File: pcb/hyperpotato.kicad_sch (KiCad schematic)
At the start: 38 parts, among them J1 Conn_01x02_Socket, J2 Conn_01x03_Pin, Q1 AO3401A, SW1 SW_Push_45deg, SW10 SW_Push_45deg, SW11 SW_Push_45deg, SW12 SW_Push_45deg, SW13 SW_Push_45deg, SW14 SW_SPDT, SW15 SW_Push, SW2 SW_Push_45deg, SW3 SW_Push_45deg, SW4 SW_Push_45deg, SW5 SW_Push_45deg, SW6 SW_Push_45deg, SW7 SW_Push_45deg, SW8 SW_Push_45deg, SW9 SW_Push_45deg, U1 Seeeduino Xiao nRF52840, U2 SK8707-01-SENSOR, U3 SK8707-01, U4 DRV2605LDGS

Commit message: Start back with e73 module
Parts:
- removed D1, D10, D11, D12, D13, D2, D3, D4, D5, D6, D7, D8, D9: D_Small, ssbb_parts:D_1206_HandSolder_reversible, symbol Device:D_Small
- removed J1: Conn_01x02_Socket, ssbb_parts:JST_PH_S2B-PH-K_Horizontal_reversible, symbol Connector:Conn_01x02_Socket
- removed SW10, SW12: SW_Push_45deg, ssbb_parts:SW_choc_v1_reversible_1u, symbol Switch:SW_Push_45deg
- removed SW13: SW_Push_45deg, ssbb_parts:SW_choc_v1_reversible_1.5u, symbol Switch:SW_Push_45deg
- removed SW14: SW_SPDT, ssbb_parts:SW_SPDT_PCM12_reversible, symbol Switch:SW_SPDT
- removed SW15: SW_Push, ssbb_parts:Panasonic_EVQPUL_EVQPUC_reversible, symbol Switch:SW_Push
- removed U1: Seeeduino Xiao nRF52840, ssbb_parts:Xiao_nRF52840_AC_Reflow_reversible, symbol PCM_marbastlib-promicroish:Seeeduino_Xiao_nRF52840
- removed U2: SK8707-01-SENSOR, ssbb_parts:Sprintek_SK8707-01_Sensor, symbol ssbb_parts:Sprintek_SK8707-01_Sensor
- removed U3: SK8707-01, symbol ssbb_parts:Sprintek_SK8707–01
- added C1, C12: 100n, Capacitor_SMD:C_0402_1005Metric, symbol Device:C_Small
- added C10, C11, C7, C8, C9: 4u7, Capacitor_SMD:C_0402_1005Metric, symbol Device:C_Small
- added C4, C5: 12p, Capacitor_SMD:C_0402_1005Metric, symbol Device:C_Small
- added C6: 1u, Capacitor_SMD:C_0402_1005Metric, symbol Device:C_Small
- added D1: BSD3C051V, Diode_SMD:D_SOD-323, symbol Device:D_TVS
- added D2: LED_ARGB, symbol Device:LED_ARGB
- added F1: 750 mA, Fuse:Fuse_0603_1608Metric, symbol Device:Fuse_Small
- added J1: HRO_TYPE-C-31-M-14, Connector_USB:USB_C_Receptacle_HRO_TYPE-C-31-M-12, symbol Connector:USB_C_Receptacle_USB2.0
- added J3: Conn_01x04_Socket, symbol Connector:Conn_01x04_Socket
- added J4: Battery, PCM_marbastlib-various:Molex_Pico-EZmate_78171-0002_1x02-1MP_P1.20mm_Vertical, symbol Connector_Generic_MountingPin:Conn_01x02_MountingPin
- added L1, L2: BLM15PX121SN1D, Inductor_SMD:L_0402_1005Metric, symbol Device:L_Small
- added L3: 10 uH, Inductor_SMD:L_0603_1608Metric, symbol Device:L_Small
- added LED1: orange, LED_SMD:LED_0402_1005Metric, symbol Device:LED_Small
- added Q2: 2N7002, Package_TO_SOT_SMD:SOT-23, symbol Transistor_FET:2N7002
- added Q3: AO3401A, Package_TO_SOT_SMD:SOT-23, symbol Transistor_FET:AO3401A
- added R1, R2: 5k1, Resistor_SMD:R_0402_1005Metric, symbol Device:R_Small
- added R10, R7: 1k5, Resistor_SMD:R_0402_1005Metric, symbol Device:R_Small
- added R11: 100R, Resistor_SMD:R_0402_1005Metric, symbol Device:R_Small
- added R12, R9: 10k, Resistor_SMD:R_0402_1005Metric, symbol Device:R_Small
- added R13, R14: 4.7k, symbol Device:R_Small
- added R15: 100k, Resistor_SMD:R_0402_1005Metric, symbol Device:R_Small
- added R16: 2M, Resistor_SMD:R_0805_2012Metric, symbol Device:R_Small
- added R17, R18, R19: 1k5, symbol Device:R_Small
- added R3, R4: 5.1k, symbol Device:R_Small
- added R6: 47k, Resistor_SMD:R_0402_1005Metric, symbol Device:R_Small
- added R8: 3k9, Resistor_SMD:R_0402_1005Metric, symbol Device:R_Small
- added SW1: RST, PCM_marbastlib-various:SW_SPST_SKQG_WithStem, symbol Switch:SW_Push_45deg
- added SW14, SW2, SW8: SW_Push_45deg, symbol Switch:SW_Push_45deg
- added SW15: PWR, PCM_marbastlib-various:SW_MSK12C02-HB, symbol Switch:SW_Push_SPDT
- added U1: nRF52840_E73-2G4M08S1C, PCM_marbastlib-various:nRF52840_E73-2G4M08S1C, symbol PCM_marbastlib-various:nRF52840_E73-2G4M08S1C
- added U3: SRV05-4, Package_TO_SOT_SMD:SOT-23-6, symbol Power_Protection:SRV05-4
- added U4: BQ24075, Package_DFN_QFN:VQFN-16-1EP_3x3mm_P0.5mm_EP1.6x1.6mm, symbol Battery_Management:BQ24075RGT
- added U5: SK8707-01, symbol ssbb_parts:Sprintek_SK8707–01
- added U6: SK8707-01-SENSOR, ssbb_parts:Sprintek_SK8707-01_Sensor, symbol ssbb_parts:Sprintek_SK8707-01_Sensor
- added U7: MAX17048, Package_DFN_QFN:DFN-8-1EP_2x2mm_P0.5mm_EP0.7x1.3mm, symbol marbastlib-various:MAX17048
- added Y1: 32.768 KHz, Crystal:Crystal_SMD_2012-2Pin_2.0x1.2mm, symbol Device:Crystal_Small
- C2: renamed from C1; footprint ssbb_parts:C_1206_HandSolder_reversible -> (none)
- C3: renamed from C2; footprint ssbb_parts:C_1206_HandSolder_reversible -> (none)
- J2: value Conn_01x03_Pin -> ELV1411A
- SW10: renamed from SW8; footprint ssbb_parts:SW_choc_v1_reversible_1u -> (none)
- SW11, SW5, SW7: footprint ssbb_parts:SW_choc_v1_reversible_1u -> (none)
- SW12: renamed from SW4; footprint ssbb_parts:SW_choc_v1_reversible_1u -> (none)
- SW13: renamed from SW9; footprint ssbb_parts:SW_choc_v1_reversible_1u -> (none)
- SW3: renamed from SW1; footprint ssbb_parts:SW_choc_v1_reversible_1u -> (none)
- SW4: renamed from SW6; footprint ssbb_parts:SW_choc_v1_reversible_1u -> (none)
- SW6: renamed from SW2; footprint ssbb_parts:SW_choc_v1_reversible_1u -> (none)
- SW9: renamed from SW3; footprint ssbb_parts:SW_choc_v1_reversible_1u -> (none)
- renumbered R1 to R5, U4 to U2
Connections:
- net +3.3V: now also C6.1, D2.1 (A), J3.2 (Pin_2), L3.2, U1.19 (VDD)
- net +3V3: now also Q3.2 (S)
- net COL0: no longer SW5.1
- net COL1: no longer SW3.1, SW4.1
- net COL2: no longer SW11.1, SW6.1, SW7.1
- net COL3: no longer SW10.1, SW9.1
- net COL4: no longer SW12.1, SW13.1
- net GND: now also SW10.2, SW11.2, SW12.2, SW13.2, SW3.2, SW4.2, SW5.2, SW6.2, SW7.2, SW9.2, C1.2, C10.2, C11.2, C12.1, C4.2, C5.2, C6.2, C7.2, C8.2, C9.2, D1.1 (A1), J3.1 (Pin_1), J4.2 (Pin_2), J4.MP (MountPin), L1.2, Q2.2 (S), R1.1, R12.2, R16.1, R2.1, R6.2, R7.2, R8.2, R9.2, SW1.2, SW14.2, SW15.3 (C), SW2.2, SW8.2, U1.21 (GND), U1.24 (GND), U1.5 (GND), U3.2 (VN), U4.17 (VSS), U4.4 (~{CE}), U4.5 (EN2), U4.8 (VSS), U5.1 (GND), U7.1 (CTG), U7.4 (GND), U7.6 (QSTRT), U7.9 (GND); no longer U2.4 (IN/TRIG)
- net ROW1: no longer SW5.2
- net SCL: now also R4.2, U7.7 (SCL)
- net SDA: now also R3.2, U7.8 (SDA)
- net TP_CLK: now also R14.2, U5.3 (CLK)
- net TP_DATA: now also R13.2, U5.2 (DATA)
- net TP_S1: now also U5.9 (S1), U6.1 (S1)
- net TP_S2: now also U5.10 (S2), U6.2 (S2)
- net TP_S3: now also U5.11 (S3), U6.3 (S3)
- net TP_S4: now also U5.12 (S4), U6.4 (S4)
- net +3.3V_OPTIONAL renamed +3.3V_HAPTIC
- net +3.3V_HAPTIC: now also R3.1, R4.1
- net POWER_CUTOFF renamed HAPTIC_CUTOFF
- new net: J1.A5 (CC1), R2.2
- new net: C5.1, U1.13 (P0.01/XL2), Y1.1
- new net: C4.1, U1.11 (P0.00/XL1), Y1.2
- new net: F1.1, L2.2
- new net: J1.B5 (CC2), R1.2
- new net: Q2.1 (G), R11.2, R12.1
- new net: D2.2 (RK), R17.2
- new net: LED1.1 (K), R10.1
- new net: R10.2, U4.9 (~{CHG})
- new net: D2.3 (GK), R18.2
- new net: D2.4 (BK), R19.2
- new net: R15.2, SW15.1 (A)
- new net: R9.1, U4.1 (TS)
- new net: R8.1, U4.16 (ISET)
- new net +3.3V_TP: Q3.3 (D), R13.1, R14.1, U5.5 (VCC)
- new net +5V: C7.1, C8.1, F1.2, R11.1, U1.27 (VBUS), U3.5 (VP), U4.13 (IN)
- new net +BATT: C10.1, C12.2, J4.1 (Pin_1), R15.1, U4.2 (BAT), U4.3 (BAT), U7.2 (CELL), U7.3 (VDD)
- new net +VSW: C11.1, C9.1, LED1.2 (A), U1.23 (VDDH), U4.10 (OUT), U4.11 (OUT), U4.6 (EN1)
- new net ALERT: U7.5 (~{ALRT})
- new net DCCH: L3.1, U1.25 (DCCH)
- new net Earth: C1.1, D1.2 (A2), J1.A1 (GND), J1.A12 (GND), J1.B1 (GND), J1.B12 (GND), J1.S1 (SHIELD), L1.1
- new net HAPTIC_TRIGGER: U2.4 (IN/TRIG)
- new net ILIM: R7.1, U4.12 (ILIM)
- new net P.1.10: U1.2 (P1.10)
- new net P0.02: U1.7 (P0.02/AIN0)
- new net P0.03: U1.3 (P0.03/AIN1)
- new net P0.04: U1.18 (P0.04/AIN2)
- new net P0.05: U1.15 (P0.05/AIN3)
- new net P0.06: U1.14 (P0.06)
- new net P0.07: U1.22 (P0.07)
- new net P0.08: U1.16 (P0.08)
- new net P0.09: U1.41 (P0.09/NFC1)
- new net P0.10: U1.43 (P0.10/NFC2)
- new net P0.12: U1.20 (P0.12)
- new net P0.13: U1.33 (P0.13)
- new net P0.15: U1.28 (P0.15)
- new net P0.17: U1.30 (P0.17)
- new net P0.20: U1.32 (P0.20)
- new net P0.22: U1.34 (P0.22)
- new net P0.24: U1.35 (P0.24)
- new net P0.26: U1.12 (P0.26)
- new net P0.28: U1.4 (P0.28/AIN4)
- new net P0.29: U1.8 (P0.29/AIN5)
- new net P0.30: U1.10 (P0.30/AIN6)
- new net P0.31: U1.9 (P0.31/AIN7)
- new net P1.00: U1.36 (P1.00)
- new net P1.02: U1.38 (P1.02)
- new net P1.04: U1.40 (P1.04)
- new net P1.06: U1.42 (P1.06)
- new net P1.09: U1.17 (P1.09)
- new net P1.11: U1.1 (P1.11)
- new net P1.13: U1.6 (P1.13)
- new net RST: SW1.1, U1.26 (P0.18/~{RESET})
- new net SW1: SW3.1
- new net SW10: SW5.1
- new net SW11: SW8.1
- new net SW12: SW11.1
- new net SW13: SW14.1
- new net SW2: SW6.1
- new net SW3: SW9.1
- new net SW4: SW12.1
- new net SW5: SW2.1
- new net SW6: SW4.1
- new net SW7: SW7.1
- new net SW8: SW10.1
- new net SW9: SW13.1
- new net SWDCLK: J3.4 (Pin_4), U1.39 (SWDCLK)
- new net SWDIO: J3.3 (Pin_3), U1.37 (SWDIO)
- new net SYSOFF: Q2.3 (D), SW15.2 (B), U4.15 (SYSOFF)
- new net TMR: R6.1, U4.14 (TMR)
- new net TP_CUTOFF: Q3.1 (G), R16.2
- new net TP_RESET: U5.4 (RST)
- new net USB-D+: J1.A6 (D+), J1.B6 (D+), U1.31 (D+), U3.6 (IO4)
- new net USB-D-: J1.A7 (D-), J1.B7 (D-), U1.29 (D-), U3.1 (IO1)
- new net USER_LED_BLUE: R19.1
- new net USER_LED_GREEN: R18.1
- new net USER_LED_RED: R17.1
- new net VBUS: J1.A4 (VBUS), J1.A9 (VBUS), J1.B4 (VBUS), J1.B9 (VBUS), L2.1
- no-connect marks 8 -> 9
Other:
- note added: "Battery management"
- note added: "External DCCH inductor for DC-DC HV input mode"
- note added: "External LF crystal for lower idle power"
- note added: "SYSOFF 1 (SW1 pos 1): Batt OFF SYSOFF 0 (SW1 pos 3): Batt ON"
- note added: "TMR: (10 x 48 s/kOhm) * 47 kOhm = 22560s = 6.27h ILIM: 1550 AOhm / 1500 Ohm = 1.03 A = 1030 mA ISET: 890 AOhm / 3900 Ohm = 0.228 A = 230 mA EN1: 1, EN2: 0 = 475 mA MAX TS: 10 kOhm to GND = no OTP"
- note added: "USB connectors and protections"
- note added: "User LED"
- note added: "Voltage sensing"
- note removed: "Battery Switch"
- note removed: "External Power Cutoff"
- note removed: "Reset"
- moved on the sheet: C2, C3, Q1, R5, SW10, SW12, SW13, SW3, SW4, SW6, SW7, SW9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

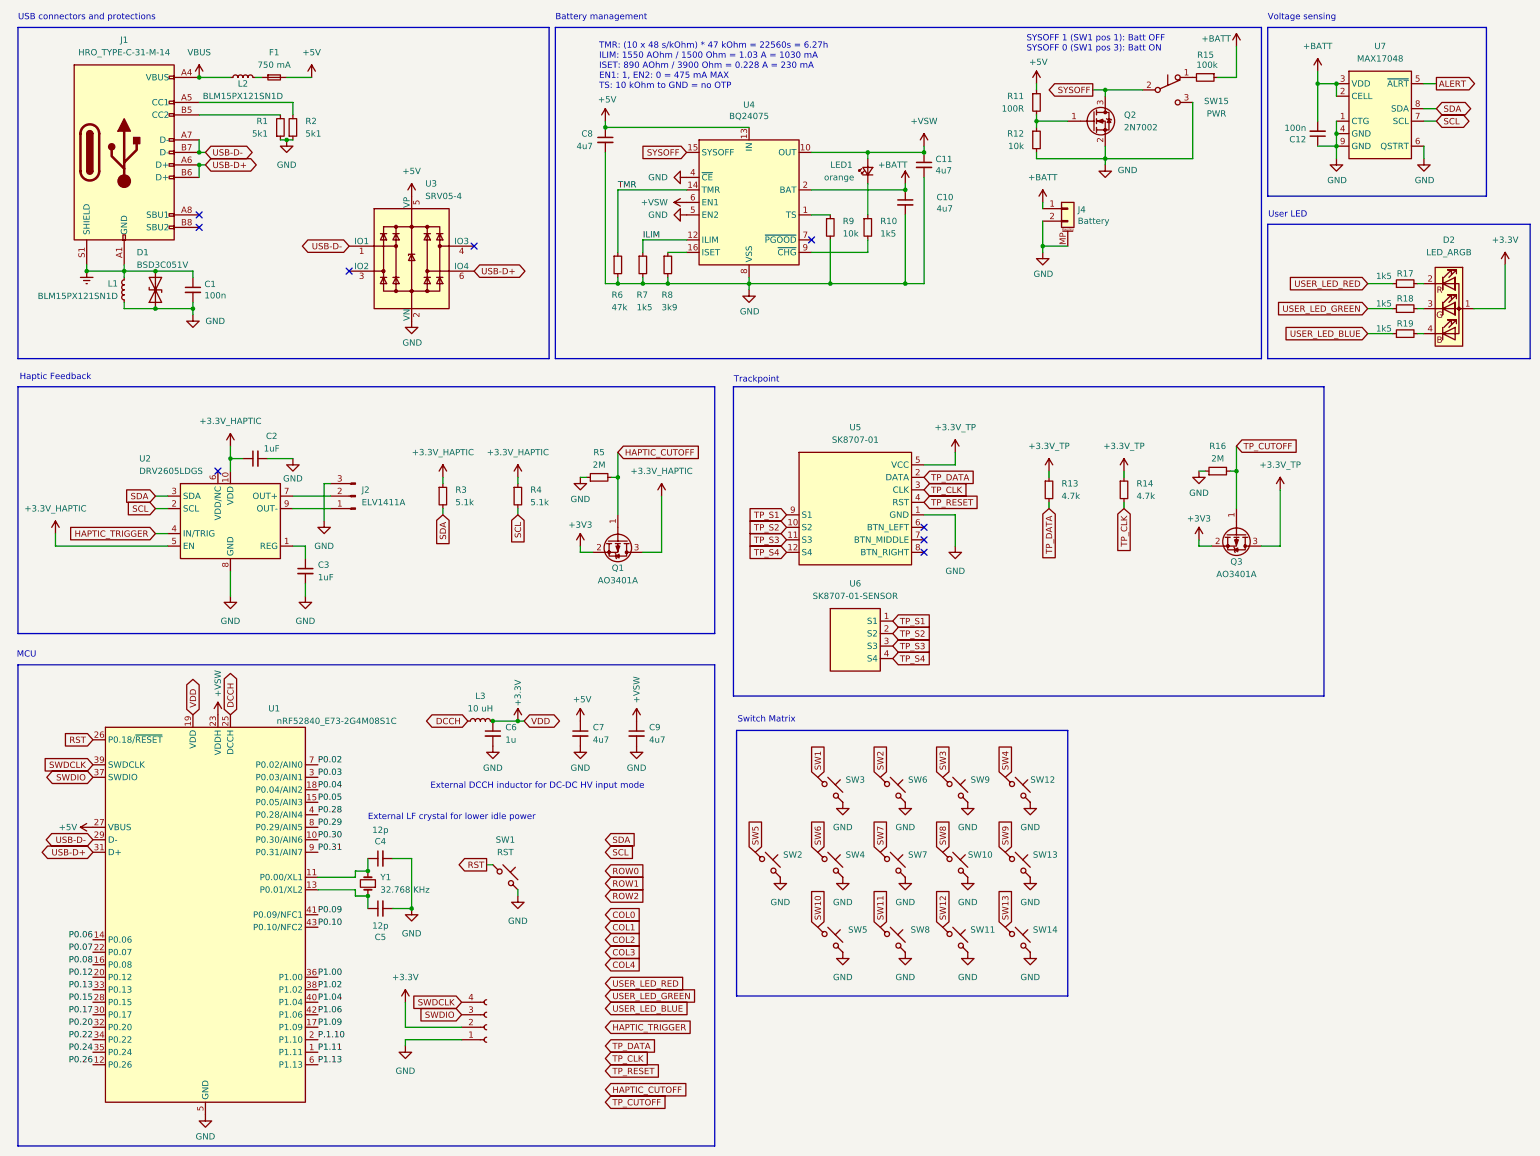
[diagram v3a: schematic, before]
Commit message: Assign footprints
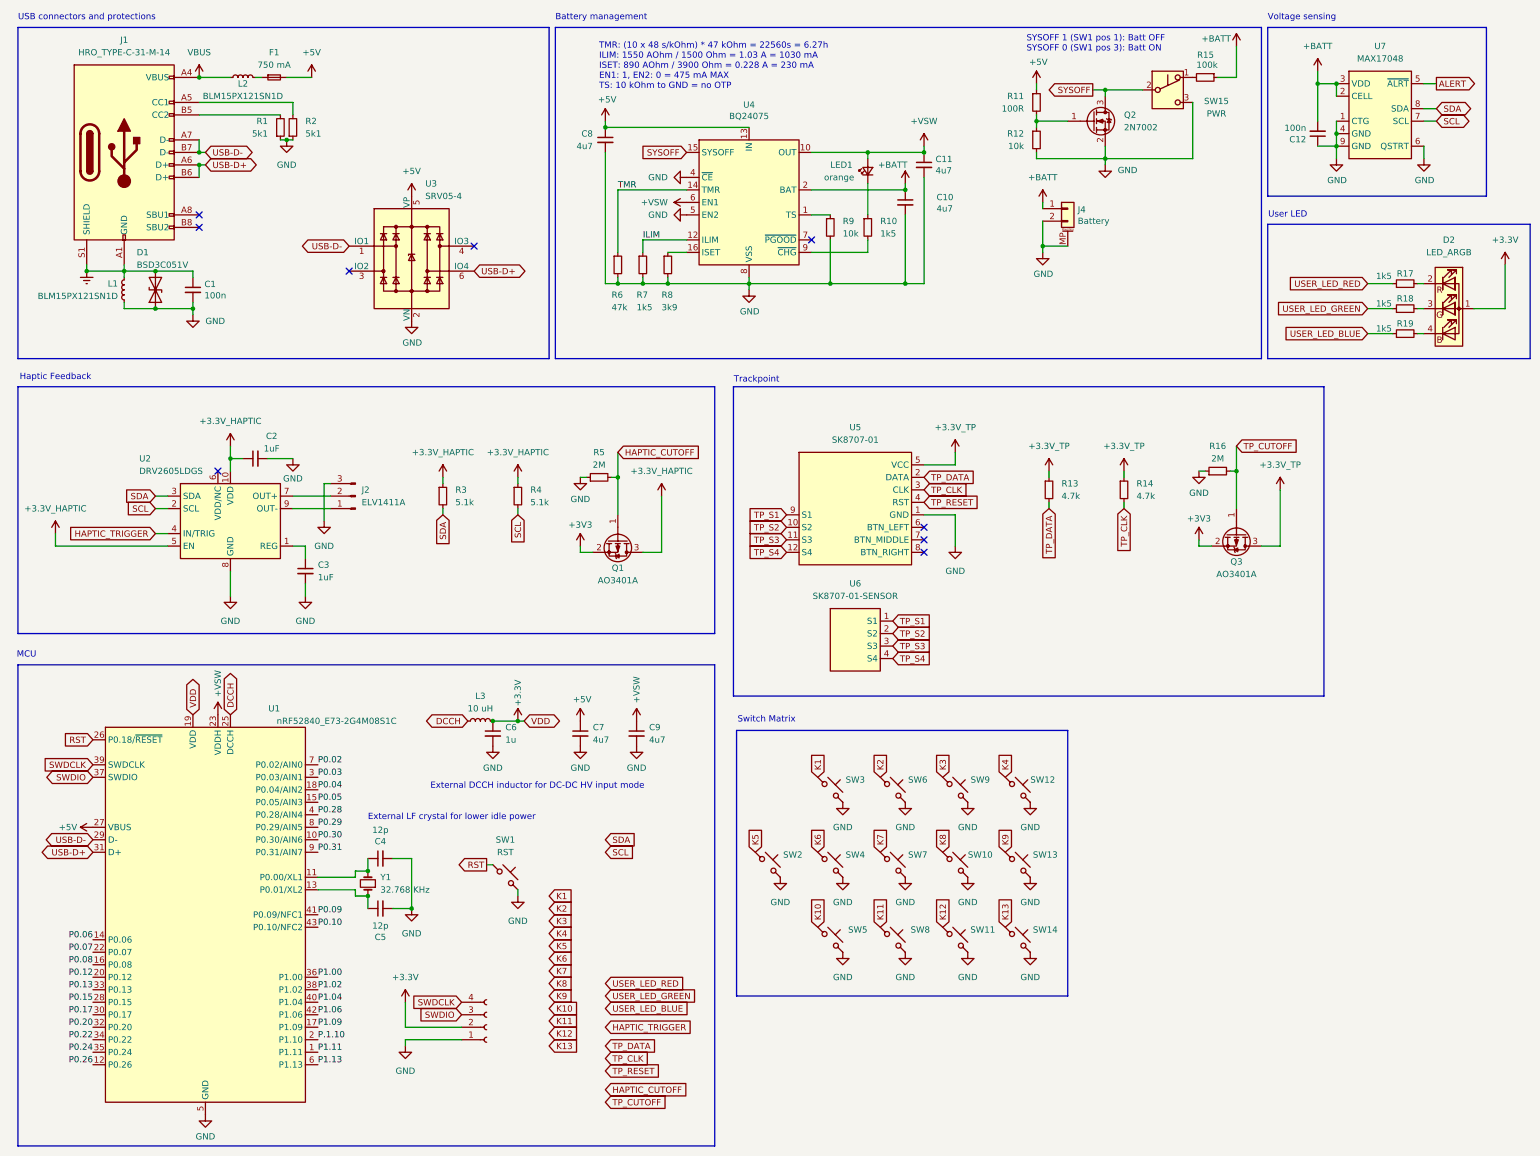
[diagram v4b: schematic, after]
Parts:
- C1, C10, C11, C12, C4, C5, C6, C7, C8, C9: footprint Capacitor_SMD:C_0402_1005Metric -> ssbb_parts:C_0603_1608Metric_reversible
- C2, C3: footprint (none) -> ssbb_parts:C_0603_1608Metric_reversible
- D1: footprint Diode_SMD:D_SOD-323 -> ssbb_parts:D_SOD-323_reversible
- F1: footprint Fuse:Fuse_0603_1608Metric -> ssbb_parts:Fuse_0603_1608Metric_reversible
- J1: footprint Connector_USB:USB_C_Receptacle_HRO_TYPE-C-31-M-12 -> ssbb_parts:USB_C_Receptacle_HRO_TYPE-C-31-M-12_reversible
- J3: footprint (none) -> Connector_PinSocket_2.54mm:PinSocket_1x04_P2.54mm_Vertical
- J4: footprint PCM_marbastlib-various:Molex_Pico-EZmate_78171-0002_1x02-1MP_P1.20mm_Vertical -> ssbb_parts:Molex_Pico-EZmate_78171-0002_1x02-1MP_P1.20mm_Vertical_reversible
- L1, L2: footprint Inductor_SMD:L_0402_1005Metric -> ssbb_parts:L_0603_1608Metric_reversible
- L3: footprint Inductor_SMD:L_0603_1608Metric -> ssbb_parts:L_0603_1608Metric_reversible
- LED1: footprint LED_SMD:LED_0402_1005Metric -> ssbb_parts:LED_0603_1608Metric_reversible
- Q1, Q2, Q3: footprint Package_TO_SOT_SMD:SOT-23 -> ssbb_parts:SOT-23_reversible
- R1, R10, R11, R12, R15, R2, R6, R7, R8, R9: footprint Resistor_SMD:R_0402_1005Metric -> ssbb_parts:R_0603_1608Metric_reversible
- R13, R14, R17, R18, R19, R3, R4: footprint (none) -> ssbb_parts:R_0603_1608Metric_reversible
- R16, R5: footprint Resistor_SMD:R_0805_2012Metric -> ssbb_parts:R_0603_1608Metric_reversible
- SW1: footprint PCM_marbastlib-various:SW_SPST_SKQG_WithStem -> ssbb_parts:Panasonic_EVQPUL_EVQPUC_reversible
- SW10, SW11, SW12, SW13, SW2, SW3, SW4, SW5, SW6, SW7, SW8, SW9: footprint (none) -> ssbb_parts:SW_choc_v1_reversible_1u
- SW14: footprint (none) -> ssbb_parts:SW_choc_v1_reversible_1.5u
- SW15: footprint PCM_marbastlib-various:SW_MSK12C02-HB -> ssbb_parts:SW_SPDT_PCM12_reversible
- U1: footprint PCM_marbastlib-various:nRF52840_E73-2G4M08S1C -> ssbb_parts:nRF52840_E73-2G4M08S1C_reversible
- U2: footprint Package_SO:VSSOP-10_3x3mm_P0.5mm -> ssbb_parts:VSSOP-10_3x3mm_P0.5mm_reversible
- U3: footprint Package_TO_SOT_SMD:SOT-23-6 -> ssbb_parts:SOT-23-6_reversible
- U4: footprint Package_DFN_QFN:VQFN-16-1EP_3x3mm_P0.5mm_EP1.6x1.6mm -> ssbb_parts:VQFN-16-1EP_3x3mm_P0.5mm_EP1.6x1.6mm_reversible
- U7: footprint Package_DFN_QFN:DFN-8-1EP_2x2mm_P0.5mm_EP0.7x1.3mm -> ssbb_parts:DFN-8-1EP_2x2mm_P0.5mm_EP0.6x1.2mm_reversible
- Y1: footprint Crystal:Crystal_SMD_2012-2Pin_2.0x1.2mm -> ssbb_parts:Crystal_SMD_2012-2Pin_2.0x1.2mm_reversible
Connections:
- net SW1 renamed K1
- net SW10 renamed K10
- net SW11 renamed K11
- net SW12 renamed K12
- net SW13 renamed K13
- net SW2 renamed K2
- net SW3 renamed K3
- net SW4 renamed K4
- net SW5 renamed K5
- net SW6 renamed K6
- net SW7 renamed K7
- net SW8 renamed K8
- net SW9 renamed K9

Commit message: wip
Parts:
- removed C1, C12: 100n, ssbb_parts:C_0603_1608Metric_reversible, symbol Device:C_Small
- removed C10, C11, C7, C8, C9: 4u7, ssbb_parts:C_0603_1608Metric_reversible, symbol Device:C_Small
- removed C4, C5: 12p, ssbb_parts:C_0603_1608Metric_reversible, symbol Device:C_Small
- removed C6: 1u, ssbb_parts:C_0603_1608Metric_reversible, symbol Device:C_Small
- removed D1: BSD3C051V, ssbb_parts:D_SOD-323_reversible, symbol Device:D_TVS
- removed D2: LED_ARGB, symbol Device:LED_ARGB
- removed F1: 750 mA, ssbb_parts:Fuse_0603_1608Metric_reversible, symbol Device:Fuse_Small
- removed J1: HRO_TYPE-C-31-M-14, ssbb_parts:USB_C_Receptacle_HRO_TYPE-C-31-M-12_reversible, symbol Connector:USB_C_Receptacle_USB2.0
- removed J3: Conn_01x04_Socket, Connector_PinSocket_2.54mm:PinSocket_1x04_P2.54mm_Vertical, symbol Connector:Conn_01x04_Socket
- removed J4: Battery, ssbb_parts:Molex_Pico-EZmate_78171-0002_1x02-1MP_P1.20mm_Vertical_reversible, symbol Connector_Generic_MountingPin:Conn_01x02_MountingPin
- removed L1, L2: BLM15PX121SN1D, ssbb_parts:L_0603_1608Metric_reversible, symbol Device:L_Small
- removed L3: 10 uH, ssbb_parts:L_0603_1608Metric_reversible, symbol Device:L_Small
- removed LED1: orange, ssbb_parts:LED_0603_1608Metric_reversible, symbol Device:LED_Small
- removed Q2: 2N7002, ssbb_parts:SOT-23_reversible, symbol Transistor_FET:2N7002
- removed Q3: AO3401A, ssbb_parts:SOT-23_reversible, symbol Transistor_FET:AO3401A
- removed R1: 5k1, ssbb_parts:R_0603_1608Metric_reversible, symbol Device:R_Small
- removed R10, R17, R18, R19, R7: 1k5, ssbb_parts:R_0603_1608Metric_reversible, symbol Device:R_Small
- removed R11: 100R, ssbb_parts:R_0603_1608Metric_reversible, symbol Device:R_Small
- removed R12, R9: 10k, ssbb_parts:R_0603_1608Metric_reversible, symbol Device:R_Small
- removed R13, R14: 4.7k, ssbb_parts:R_0603_1608Metric_reversible, symbol Device:R_Small
- removed R15: 100k, ssbb_parts:R_0603_1608Metric_reversible, symbol Device:R_Small
- removed R16: 2M, ssbb_parts:R_0603_1608Metric_reversible, symbol Device:R_Small
- removed R6: 47k, ssbb_parts:R_0603_1608Metric_reversible, symbol Device:R_Small
- removed R8: 3k9, ssbb_parts:R_0603_1608Metric_reversible, symbol Device:R_Small
- removed SW1: RST, ssbb_parts:Panasonic_EVQPUL_EVQPUC_reversible, symbol Switch:SW_Push_45deg
- removed SW14: SW_Push_45deg, ssbb_parts:SW_choc_v1_reversible_1.5u, symbol Switch:SW_Push_45deg
- removed SW15: PWR, ssbb_parts:SW_SPDT_PCM12_reversible, symbol Switch:SW_Push_SPDT
- removed SW2, SW8: SW_Push_45deg, ssbb_parts:SW_choc_v1_reversible_1u, symbol Switch:SW_Push_45deg
- removed U1: nRF52840_E73-2G4M08S1C, ssbb_parts:nRF52840_E73-2G4M08S1C_reversible, symbol PCM_marbastlib-various:nRF52840_E73-2G4M08S1C
- removed U3: SRV05-4, ssbb_parts:SOT-23-6_reversible, symbol Power_Protection:SRV05-4
- removed U4: BQ24075, ssbb_parts:VQFN-16-1EP_3x3mm_P0.5mm_EP1.6x1.6mm_reversible, symbol Battery_Management:BQ24075RGT
- removed U5: SK8707-01, symbol ssbb_parts:Sprintek_SK8707–01
- removed U6: SK8707-01-SENSOR, ssbb_parts:Sprintek_SK8707-01_Sensor, symbol ssbb_parts:Sprintek_SK8707-01_Sensor
- removed U7: MAX17048, ssbb_parts:DFN-8-1EP_2x2mm_P0.5mm_EP0.6x1.2mm_reversible, symbol marbastlib-various:MAX17048
- removed Y1: 32.768 KHz, ssbb_parts:Crystal_SMD_2012-2Pin_2.0x1.2mm_reversible, symbol Device:Crystal_Small
- added D1, D10, D11, D12, D13, D2, D3, D4, D5, D6, D7, D8, D9: D_Small, ssbb_parts:D_0603_1608Metric_reversible, symbol Device:D_Small
- added J1: Conn_01x02_Socket, ssbb_parts:Molex_Pico-EZmate_78171-0002_1x02-1MP_P1.20mm_Vertical_reversible, symbol Connector:Conn_01x02_Socket
- added R5: R_Small, ssbb_parts:R_0603_1608Metric_reversible, symbol Device:R_Small
- added SW10, SW12: SW_Push_45deg, ssbb_parts:SW_choc_v1_reversible_1u, symbol Switch:SW_Push_45deg
- added SW13: SW_Push_45deg, ssbb_parts:SW_choc_v1_reversible_1.5u, symbol Switch:SW_Push_45deg
- added SW14: SW_SPDT, ssbb_parts:SW_SPDT_PCM12_reversible, symbol Switch:SW_SPDT
- added SW15: SW_Push, ssbb_parts:Panasonic_EVQPUL_EVQPUC_reversible, symbol Switch:SW_Push
- added U1: Seeeduino Xiao nRF52840, ssbb_parts:Xiao_nRF52840_AC_Reflow_reversible, symbol PCM_marbastlib-promicroish:Seeeduino_Xiao_nRF52840
- added U2: SK8707-01-SENSOR, ssbb_parts:Sprintek_SK8707-01_Sensor, symbol ssbb_parts:Sprintek_SK8707-01_Sensor
- added U3: SK8707-01, symbol ssbb_parts:Sprintek_SK8707–01
- added U5: 74HC595, ssbb_parts:TSSOP-16_4.4x5mm_P0.65mm_reversible, symbol 74xx:74HC595
- J2: value ELV1411A -> Conn_01x03_Pin
- R2: value 5k1 -> R_Small
- R3, R4: value 5.1k -> R_Small
- renumbered C2 to C1, C3 to C2, R5 to R1, SW3 to SW1, SW6 to SW2, SW9 to SW3, SW12 to SW4, SW4 to SW6, SW10 to SW8, SW13 to SW9, U2 to U4
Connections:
- net HAPTIC_TRIGGER is gone; now on net GND: U4.4 (IN/TRIG)
- net K2 is gone; now on net COL2: SW2.1
- net K6 is gone; now on net COL1: SW6.1
- net K7 is gone; now on net COL2: SW7.1
- net K8 is gone; now on net COL3: SW8.1
- net +3.3V: now also U1.10 (3V3)
- net GND: now also J1.2 (Pin_2), SW15.2, U1.15 (BAT-), U1.22 (GND), U1.9 (GND), U3.1 (GND), U5.13 (~{OE}), U5.8 (GND); no longer R2.1, SW1.2, SW11.2, SW2.2, SW3.2, SW4.2, SW5.2, SW6.2, SW7.2, SW8.2, SW9.2
- net SCL: now also R3.2; no longer R4.2
- net SDA: now also R2.2; no longer R3.2
- net TP_CLK: now also R5.2, U3.3 (CLK)
- net TP_DATA: now also R4.2, U3.2 (DATA)
- net TP_S1: now also U2.1 (S1), U3.9 (S1)
- net TP_S2: now also U2.2 (S2), U3.10 (S2)
- net TP_S3: now also U2.3 (S3), U3.11 (S3)
- net TP_S4: now also U2.4 (S4), U3.12 (S4)
- net +3.3V_HAPTIC renamed +3.3V_OPTIONAL
- net +3.3V_OPTIONAL: now also R2.1, R5.1, U3.5 (VCC)
- net HAPTIC_CUTOFF renamed POWER_CUTOFF
- net K1 renamed COL1
- net COL1: now also SW10.1
- net K10 renamed COL0
- net K12 renamed COL2
- net K3 renamed COL3
- net COL3: now also SW12.1
- net K4: no longer names the net of SW4.1
- net K4: now also D4.2 (A)
- net K9: no longer names the net of SW9.1
- net K9: now also D9.2 (A)
- new net: D8.2 (A), SW8.2
- new net: D13.2 (A), SW13.2
- new net: D10.2 (A), SW10.2
- new net: D1.2 (A), SW1.2
- new net: D12.2 (A), SW12.2
- new net: D3.2 (A), SW3.2
- new net: D2.2 (A), SW2.2
- new net: D7.2 (A), SW7.2
- new net: D6.2 (A), SW6.2
- new net: D11.2 (A), SW11.2
- new net BAT+: SW14.3 (C), U1.16 (BAT+)
- new net COL4: SW13.1, SW4.2, SW9.2
- new net IO_CS: U5.12 (RCLK)
- new net MOSI: U5.14 (SER)
- new net RESET: SW15.1, U1.21 (RST)
- new net ROW0: D1.1 (K), D2.1 (K), D3.1 (K), D4.1 (K)
- new net ROW1: D10.1 (K), D11.1 (K), D12.1 (K), D13.1 (K), D5.1 (K), D5.2 (A), D6.1 (K), D7.1 (K), D8.1 (K), D9.1 (K), SW5.2
- new net SCK: U5.11 (SRCLK)
- new net TP_RST: U3.4 (RST)
- new net VBAT: J1.1 (Pin_1), SW14.2 (B)
- new net VCC: U5.10 (~{SRCLR}), U5.16 (VCC)
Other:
- note added: "Battery Switch"
- note added: "External Power Cutoff"
- note added: "Reset"
- note added: "SHIFT REGISTER"
- note removed: "Battery management"
- note removed: "External DCCH inductor for DC-DC HV input mode"
- note removed: "External LF crystal for lower idle power"
- note removed: "SYSOFF 1 (SW1 pos 1): Batt OFF SYSOFF 0 (SW1 pos 3): Batt ON"
- note removed: "TMR: (10 x 48 s/kOhm) * 47 kOhm = 22560s = 6.27h ILIM: 1550 AOhm / 1500 Ohm = 1.03 A = 1030 mA ISET: 890 AOhm / 3900 Ohm = 0.228 A = 230 mA EN1: 1, EN2: 0 = 475 mA MAX TS: 10 kOhm to GND = no OTP"
- note removed: "USB connectors and protections"
- note removed: "User LED"
- note removed: "Voltage sensing"
- moved on the sheet: C1, C2, Q1, R1, SW1, SW2, SW3, SW4, SW6, SW7, SW8, SW9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
